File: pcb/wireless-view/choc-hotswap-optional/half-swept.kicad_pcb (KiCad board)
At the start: 2 copper layers, 113.3 x 89.7 mm, 26 parts, among them J1 JST-BATTERY, SW1 SW_Push, SW10 SW_Push, SW11 SW_Push, SW12 SW_Push, SW13 SW_DPDT, SW14 SW_Push, SW15 SW_Push, SW16 SW_Push, SW17 SW_Push, SW18 SW_Push, SW2 SW_Push, SW20 SW_Push, SW21 SW_Push, SW3 SW_Push, SW4 SW_Push, SW5 SW_Push, SW6 SW_Push, SW7 SW_DPDT, SW8 SW_Push, SW9 SW_Push, U1 nice_nano

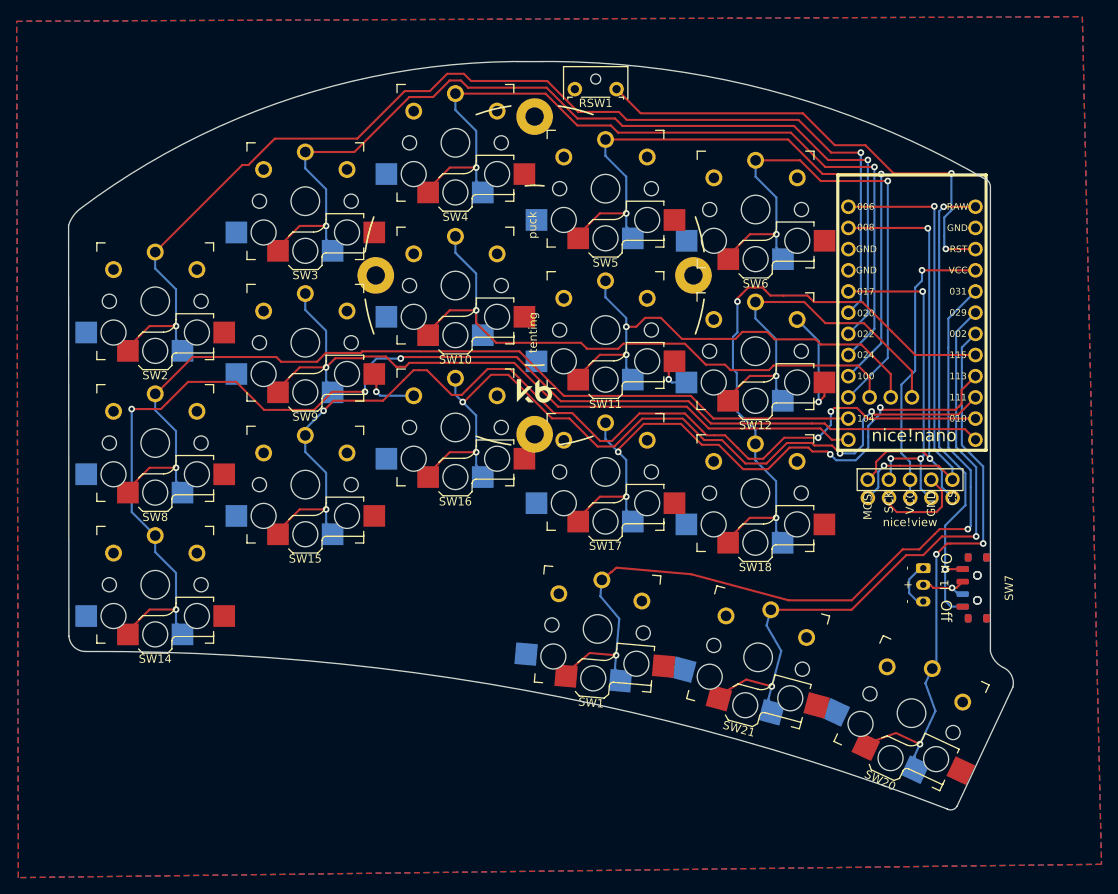
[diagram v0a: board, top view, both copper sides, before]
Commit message: updated wireless sweeeeeep to support mill-max as well
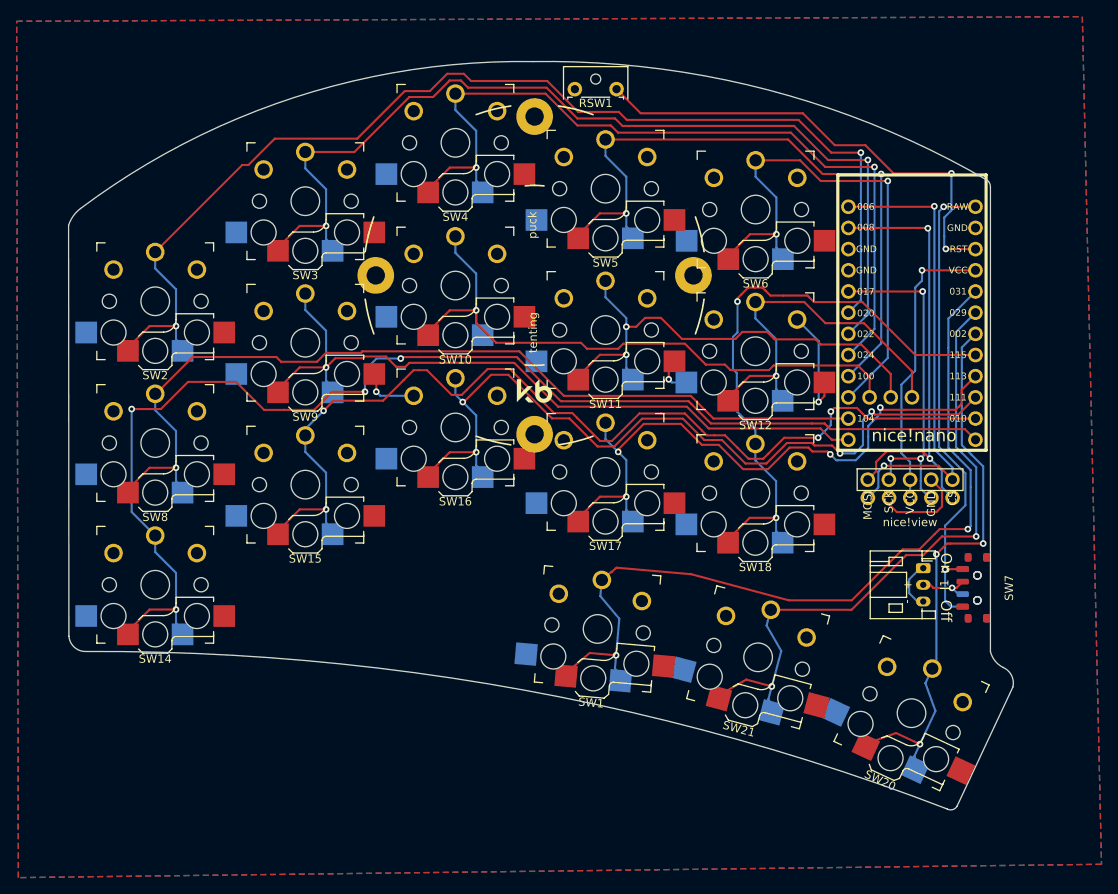
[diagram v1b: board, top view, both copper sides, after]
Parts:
- SW1, SW10, SW11, SW12, SW14, SW15, SW16, SW17, SW18, SW2, SW20, SW21, SW3, SW4, SW5, SW6, SW8, SW9: footprint fingerpunch:Kailh_socket_PG1350_optional_reversible -> fingerpunch:Kailh_socket_PG1350_optional_reversible_millmax

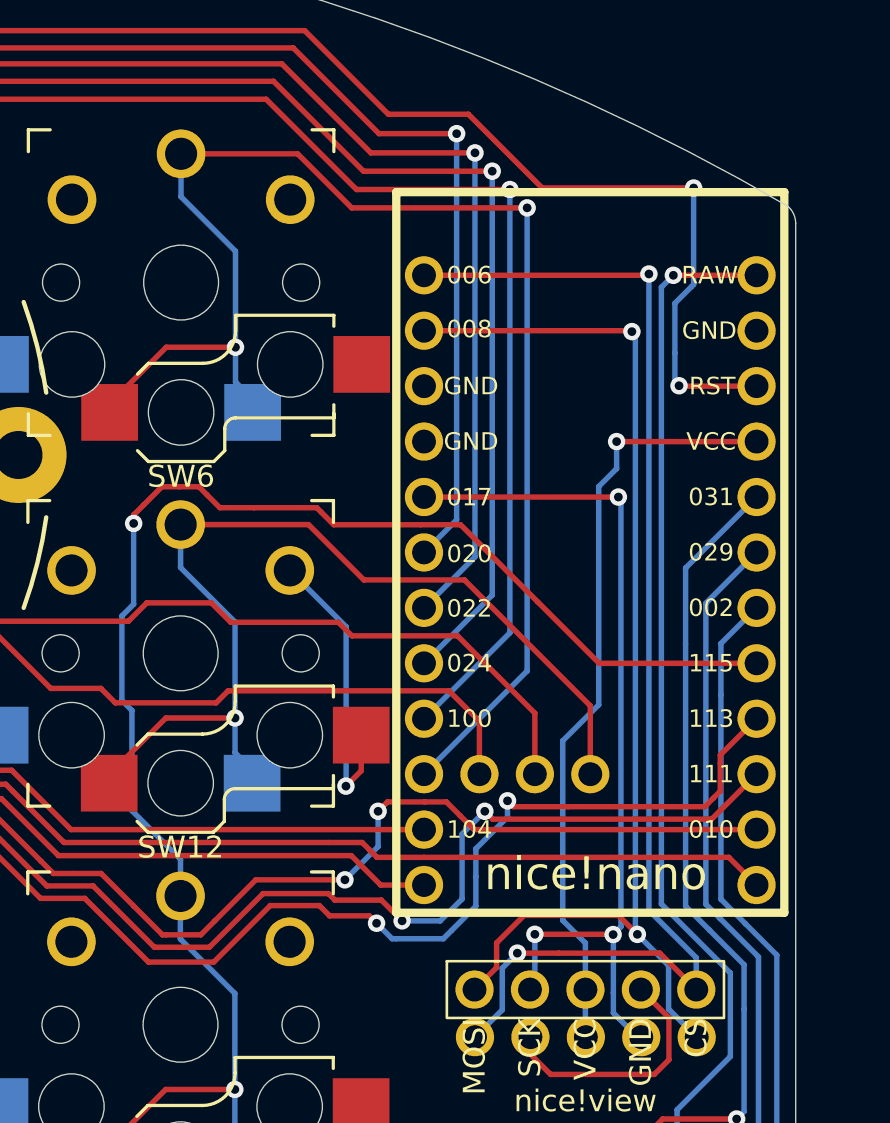
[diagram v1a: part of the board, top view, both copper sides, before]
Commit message: Change n!n pin assigmnets to match ZMK's nice_view_adapter
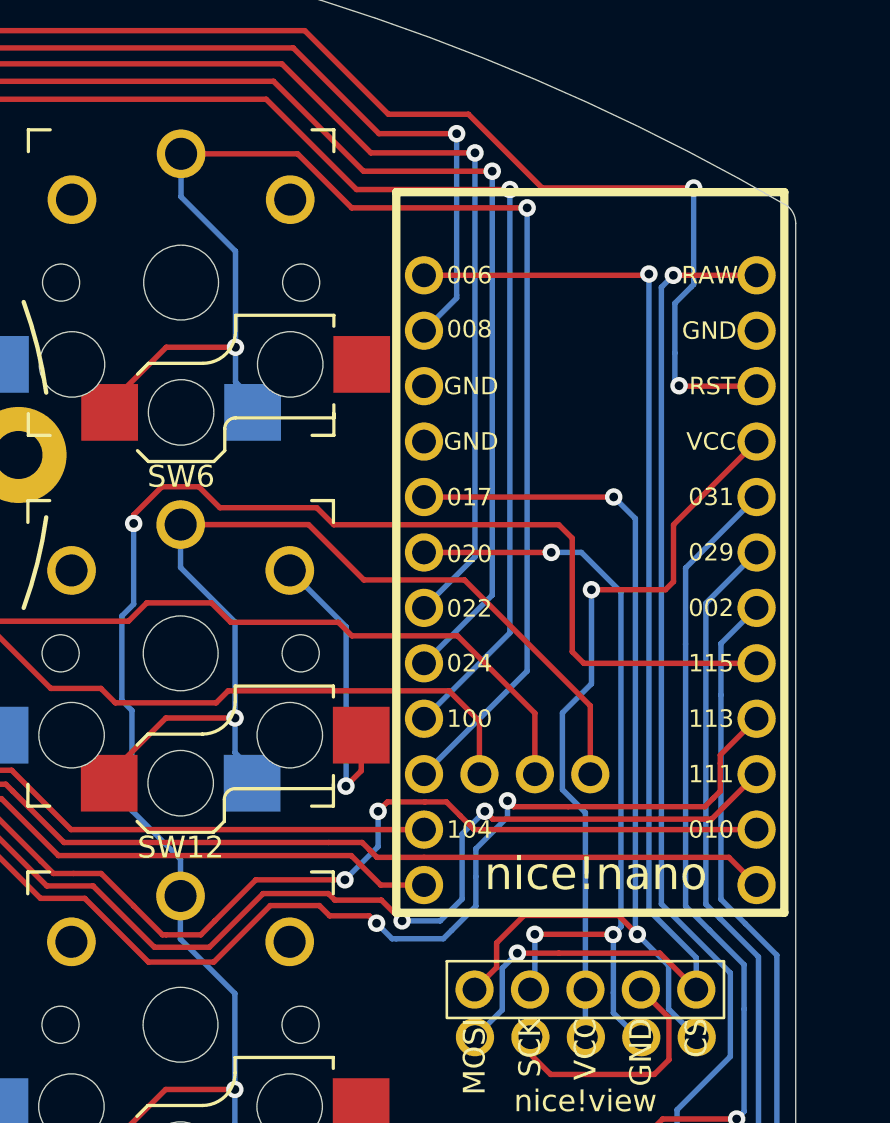
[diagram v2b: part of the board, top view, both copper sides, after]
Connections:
- U1 pad 2: mosi -> Switch1
- U1 pad 5: sck -> mosi
- U1 pad 6: Switch1 -> sck
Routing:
- net Switch1: track 137.6 -> 127.5 mm
- net mosi: track 53.0 -> 44.9 mm
- net sck: track 40.7 -> 37.2 mm
- net Switch15: track 71.7 -> 74.7 mm
- net vcc: track 35.2 -> 33.4 mm
